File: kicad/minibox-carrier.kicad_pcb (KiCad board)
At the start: 4 copper layers, 94.5 x 117 mm, 20 parts, among them J1 ESP32-S3 J1 - USB LEFT, J2 ESP32-S3 J3 - USB LEFT, J3 INMP441 two 1x3 sockets, J4 MAX98357A module socket, J5 PCF8563T upright module, J6 ST7796 14-pin display, J7 WJ500V-5.08-03P-14-00A, J8 WJ500V-5.08-2P, J9 WJ500V-5.08-2P, SW1 CPG151101D13, SW2 CPG151101D13, SW3 CPG151101D13, SW4 CPG151101D13

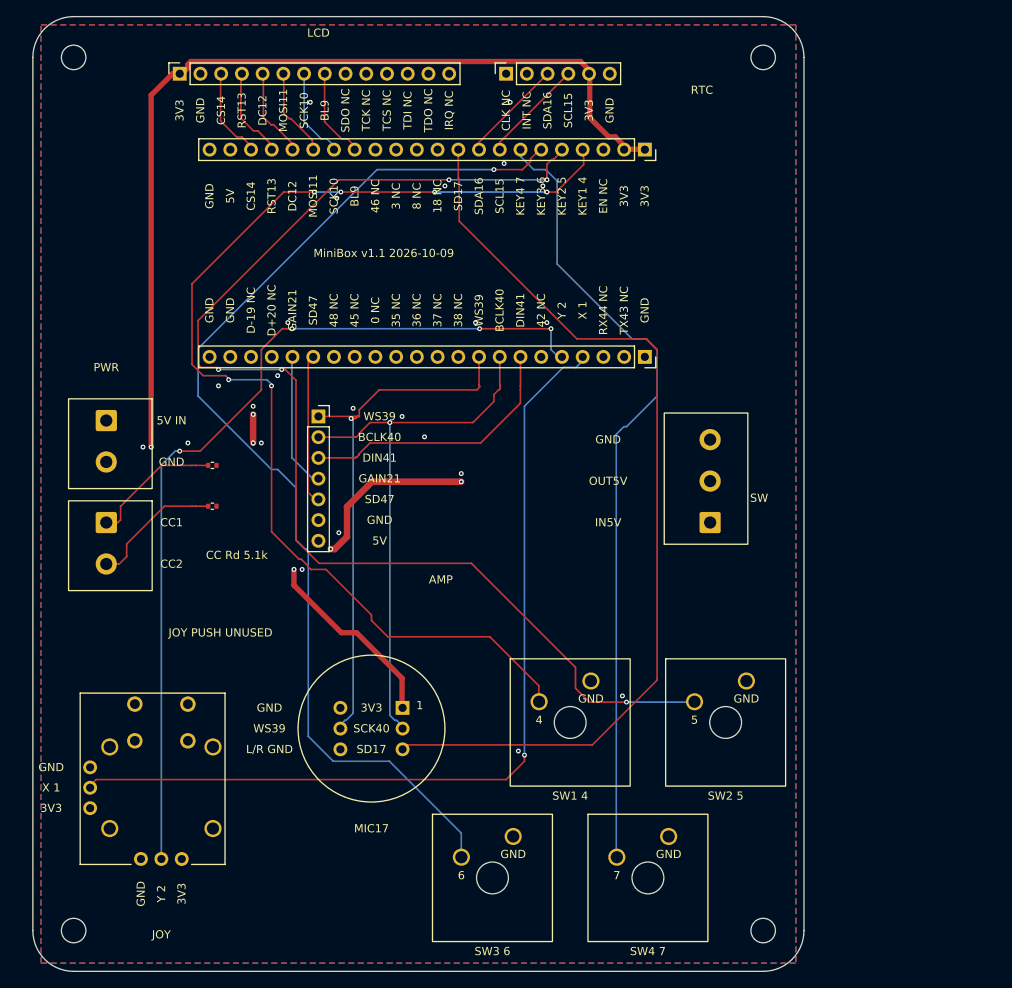
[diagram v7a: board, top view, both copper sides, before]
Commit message: Correct carrier GPIO wiring and regenerate JLC review files
Correct RTC signal identities without changing routed geometry; move amplifier GAIN to42 and microphone SD to21; leave17 NC. Correct microphone pin order, revise controls and power terminal placement, and keep joystick pad copper1.22mm from the left pour boundary. Prune18 redundant ground vias and regenerate all CAM, factory placements, renders and hash-verified review packages. Record official44-pad GPIO audit and the pending JLC submission/factory checks.

Co-authored-by: Copilot App <223556219+Copilot@users.noreply.github.com>
Copilot-Session: d5123da0-77f3-46dc-9275-266fb44de942
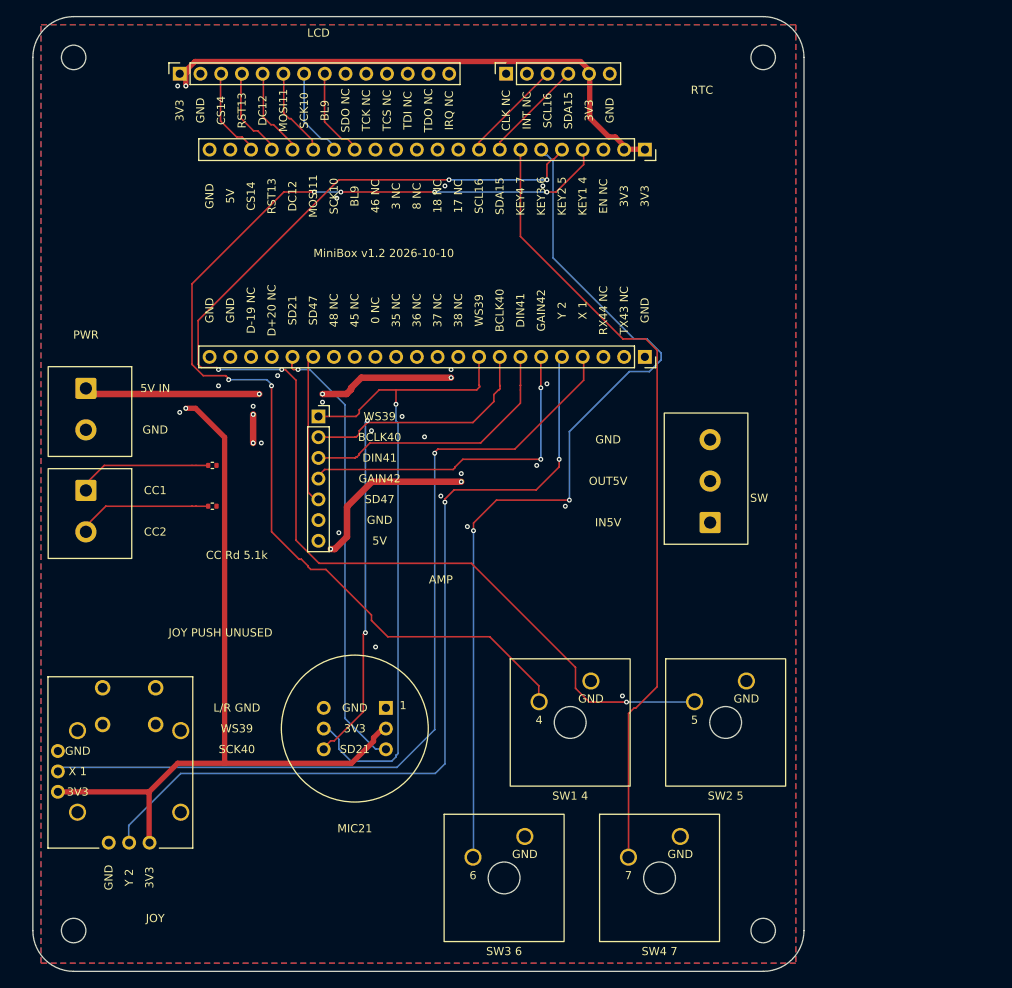
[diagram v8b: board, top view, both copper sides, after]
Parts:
- moved J8 4.67 mm to (11.5, 48.6)
- moved J9 4.67 mm to (11.5, 61.1)
- moved JS1 4.43 mm to (16.8, 95.5)
- moved J3 2.05 mm to (48.3, 87.7)
- moved SW3 1.43 mm to (62.7, 108.5)
- moved SW4 1.42 mm to (81.8, 108.5)
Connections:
- J1 pad 10: MIC_SD -> (no net)
- J1 pad 8: RTC_SCL -> RTC_SDA
- J1 pad 9: RTC_SDA -> RTC_SCL
- J2 pad 18: AMP_GAIN -> MIC_SD
- J2 pad 6: (no net) -> AMP_GAIN
- J3 pad 1: 3V3 -> GND
- J3 pad 3: I2S_BCLK -> 3V3
- J3 pad 6: GND -> I2S_BCLK
- J5 pad 3: RTC_SDA -> RTC_SCL
- J5 pad 4: RTC_SCL -> RTC_SDA
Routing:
- net MIC_SD: track 114.9 -> 54.8 mm, vias 0 -> 1
- net AMP_GAIN: track 16.7 -> 41.1 mm, vias 0 -> 2
- net BUTTON3: track 132.7 -> 110.3 mm, vias 1 -> 2
- net I2S_WS: track 65.5 -> 81.8 mm
- net 3V3: track 216.9 -> 203.4 mm
- net 5V_IN: track 84.8 -> 93.0 mm, vias 0 -> 3
- net I2S_BCLK: track 67.5 -> 72.5 mm, vias 1 -> 2
- net GPIO2: track 110.2 -> 105.8 mm, vias 4 -> 2
- net BUTTON4: track 98.0 -> 97.0 mm
- net GPIO1: track 108.3 -> 107.3 mm
- net USB_CC2: track 16.3 -> 16.9 mm
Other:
- board text added: "17 NC"
- board text added: "GAIN42"
- board text added: "MIC21"
- board text added: "MiniBox v1.2 2026-10-10"
- board text added: "SCL16"
- board text added: "SD21"
- board text added: "SDA15"
- board text removed: "42 NC"
- board text removed: "GAIN21"
- board text removed: "MIC17"
- board text removed: "MiniBox v1.1 2026-10-09"
- board text removed: "SCL15"
- board text removed: "SD17"
- board text removed: "SDA16"
